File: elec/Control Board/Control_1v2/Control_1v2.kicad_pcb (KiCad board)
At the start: 2 copper layers, 205 x 190 mm, 348 parts, among them J1 DB9_Female_MountingHoles, J10 Conn_02x12_Odd_Even, J11 Con_01x02_2.5mm, J12 Con_01x02_2.5mm, J13 Con_01x02_2.5mm, J14 Conn_01x10, J15 DB25_Female_MountingHoles, J16 Conn_01x04, J17 Conn_01x05, J18 Conn_01x04, J19 Conn_01x07, J2 Conn_01x08, J20 Conn_01x04_KK-254_0470531000, J201 Con_01x02_2.5mm, J23 0.100_2Pin, J24 Conn_01x04, J25 Con_01x02_2.5mm, J26 Conn_01x10, J27 Conn_02x12_Odd_Even, J28 Con_01x02_2.5mm, J29 Conn_01x10, J3 Conn_01x08, J30 Con_01x02_2.5mm, J31 Con_01x02_2.5mm, J32 Con_01x02_2.5mm, J33 Con_01x02_2.5mm, J34 Con_01x02_2.5mm, J35 Conn_02x05_Odd_Even, J36 Conn_02x05_Odd_Even, J37 Conn_01x04, J38 Conn_02x06_Odd_Even, J39 Conn_02x06_Odd_Even, J4 Conn_01x08, J40 Conn_02x06_Odd_Even, J41 Conn_02x06_Odd_Even, J42 Conn_02x06_Odd_Even, J43 Conn_01x30, J44 Conn_01x30, J45 Conn_01x30, J46 Conn_01x30, J47 Conn_01x30, J48 Conn_01x30, J49 Conn_01x30, J5 Conn_01x08, J50 Conn_01x30, J51 Conn_01x30, J52 Conn_01x30, J53 Conn_01x30, J54 Conn_01x30, J55 Conn_02x06_Odd_Even, J56 Conn_02x06_Odd_Even, J57 Conn_02x06_Odd_Even, J58 Conn_02x06_Odd_Even, J59 Conn_02x06_Odd_Even, J6 Conn_01x08, J7 Conn_01x10, J8 Conn_02x18_Odd_Even, J801 Conn_01x03_0.1", J802 Con_01x02_0.1", J803 Screw_Terminal_01x04_5.08mm, J804 Screw_Terminal_01x02_5.08mm, J805 Con_01x02_0.1", J9 Conn_01x10, K801 Relay SRU-12VDC, Q1 BSS138, Q10 BSS138, Q11 BSS138, Q12 BSS138, Q13 BSS138, Q14 BSS138, Q2 NCE01P30K, Q3 BSS138, Q4 BSS138, Q801 BSS138, Q9 BSS138

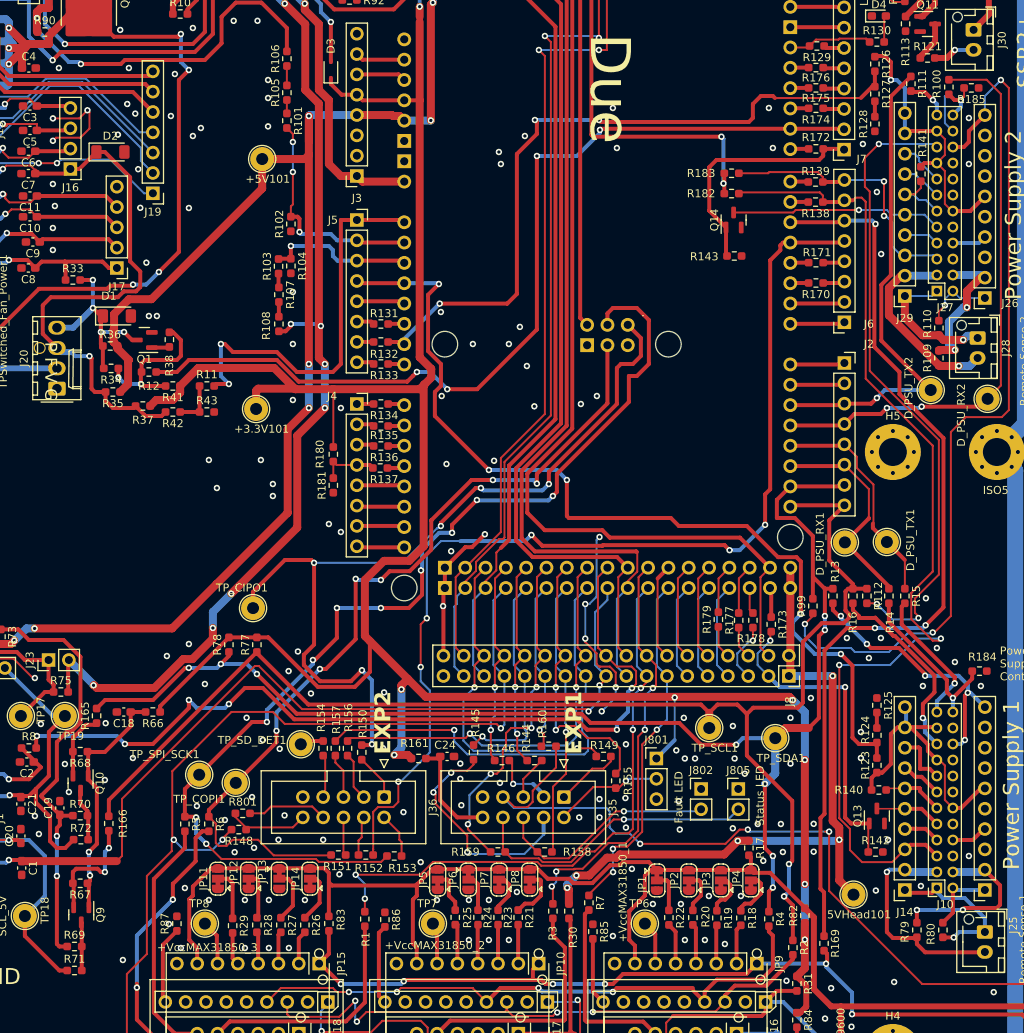
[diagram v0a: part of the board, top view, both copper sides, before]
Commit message: PCB V1.2. Set to ignore many silk screen errors. Only three errors left.
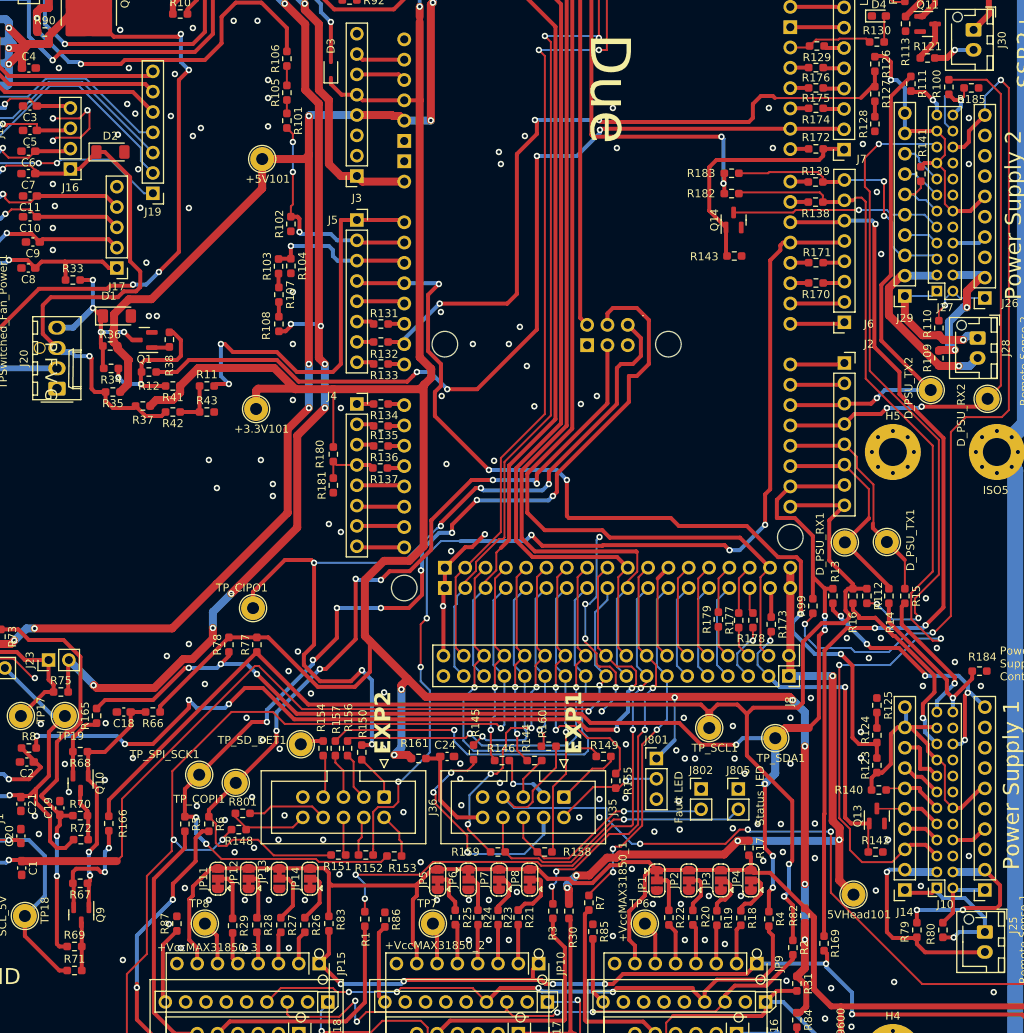
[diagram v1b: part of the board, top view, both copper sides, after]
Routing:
- net +5V: track 395.0 -> 391.8 mm
- net /Display Interface/LED_Green: track 101.5 -> 100.4 mm
